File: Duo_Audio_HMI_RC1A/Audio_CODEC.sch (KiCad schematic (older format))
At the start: 38 parts

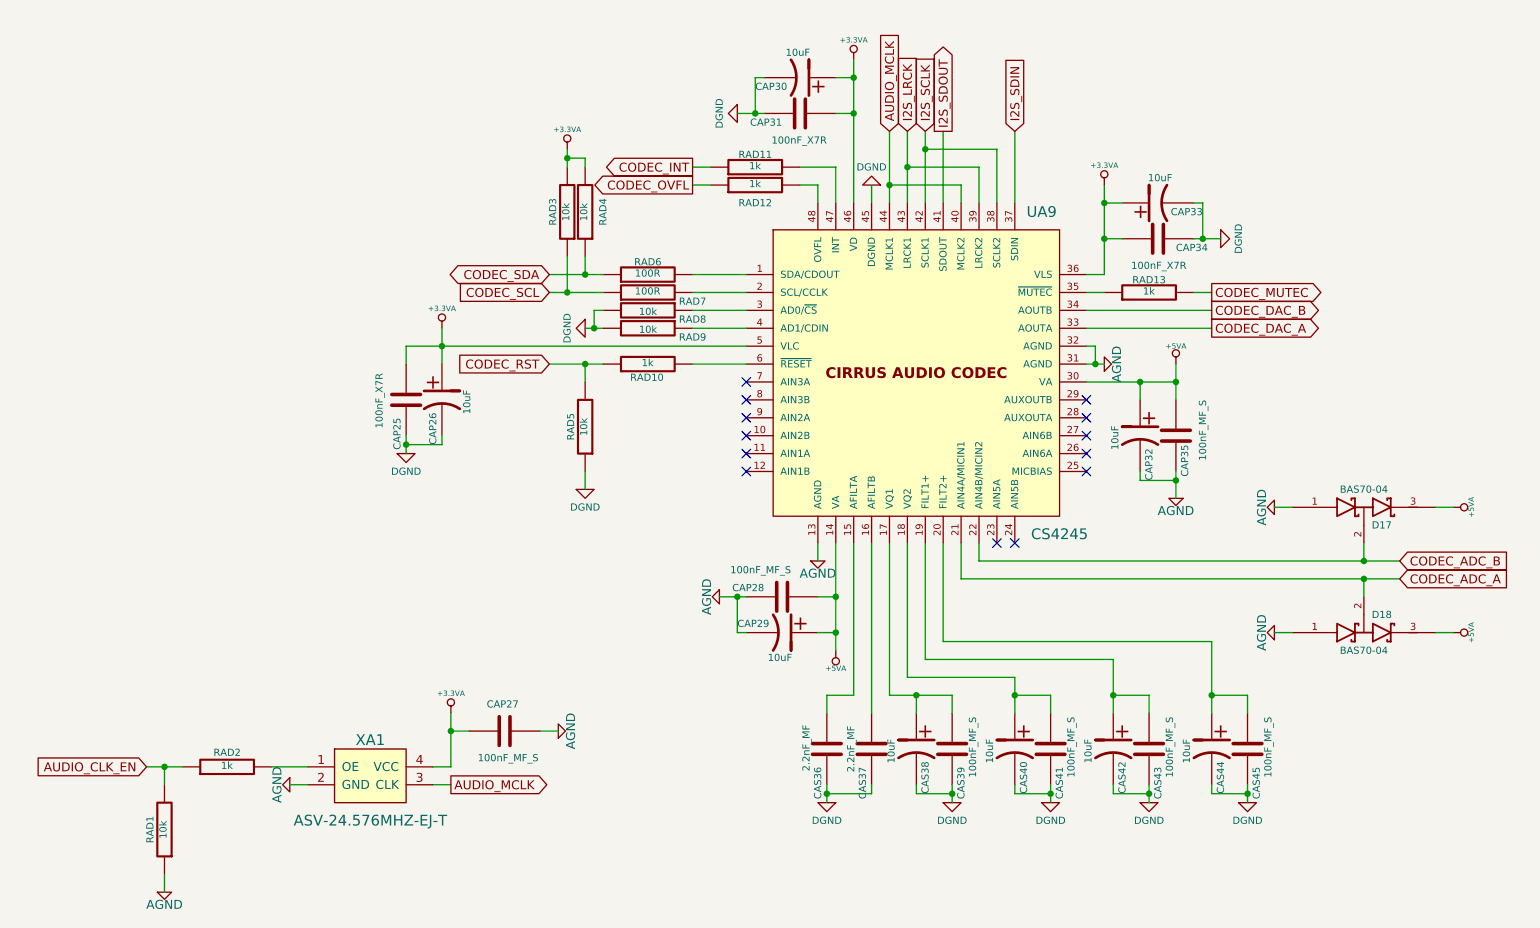
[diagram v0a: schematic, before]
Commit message: Finished RCA1 schematic of the Baseboard and the Pannelboard with USB OTG. Board dimensions, most footprint attribution and major placement implemented in layout. Learning GIT!
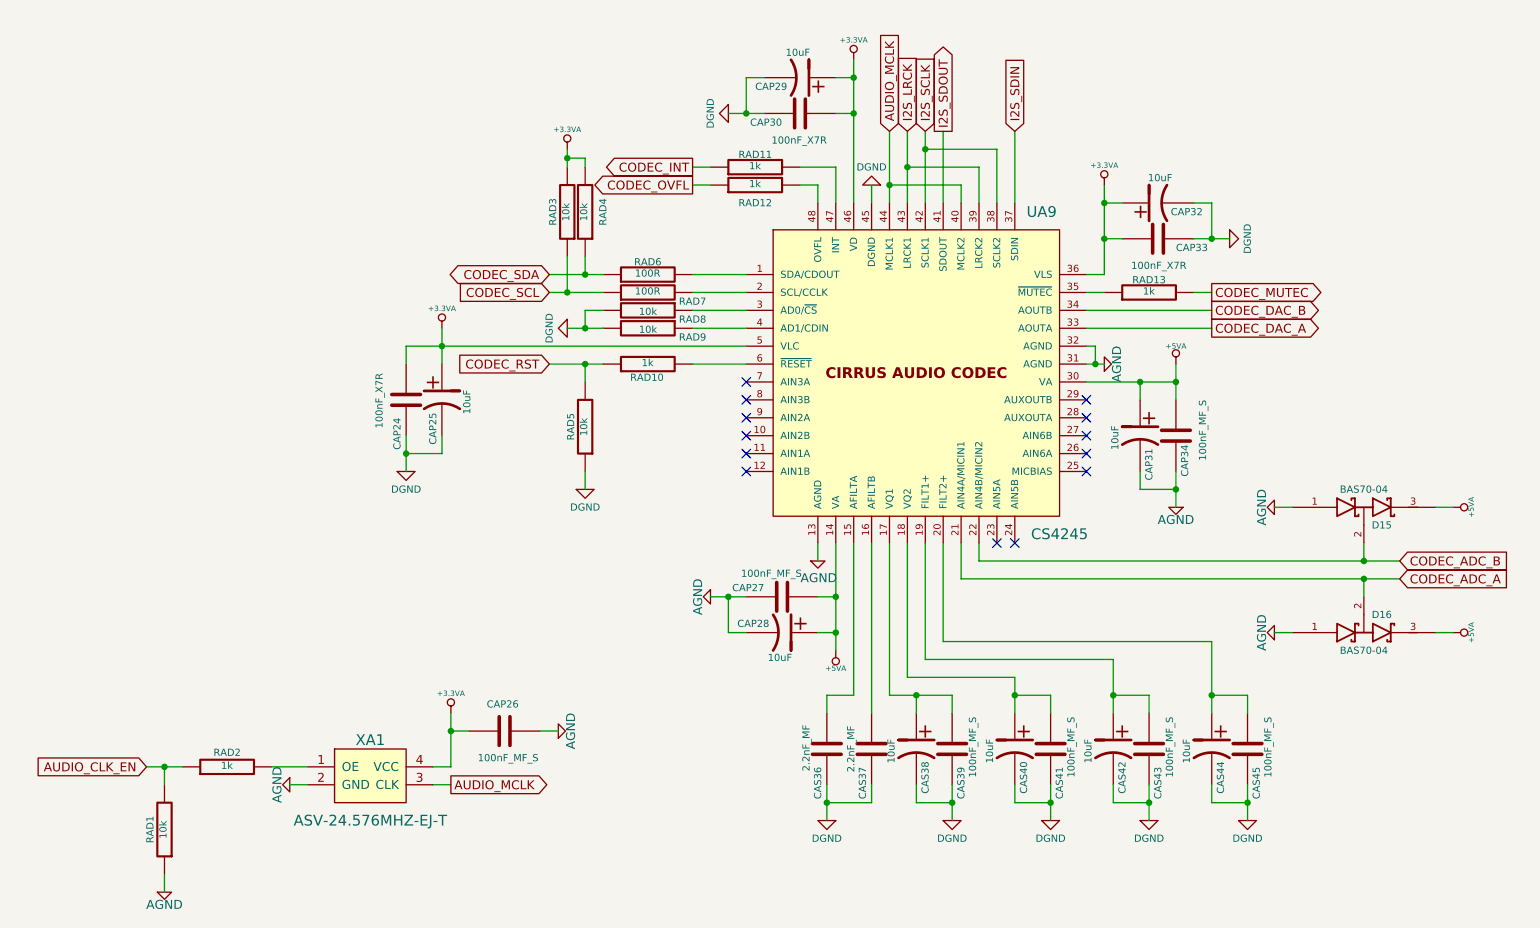
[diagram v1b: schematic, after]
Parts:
- renumbered CAP25 to CAP24, CAP26 to CAP25, CAP27 to CAP26, CAP28 to CAP27, CAP29 to CAP28, CAP30 to CAP29, CAP31 to CAP30, CAP32 to CAP31, CAP33 to CAP32, CAP34 to CAP33, CAP35 to CAP34, D17 to D15, D18 to D16
